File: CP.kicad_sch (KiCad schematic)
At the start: 26 parts, among them J5 Screw_Terminal_01x03, U11 OPA2991IDR, U6 OPA2991IDR

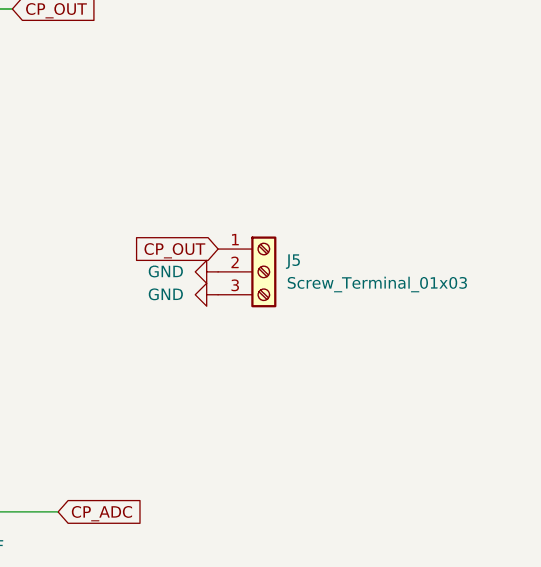
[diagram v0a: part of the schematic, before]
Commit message: 1st test board manufacturing files
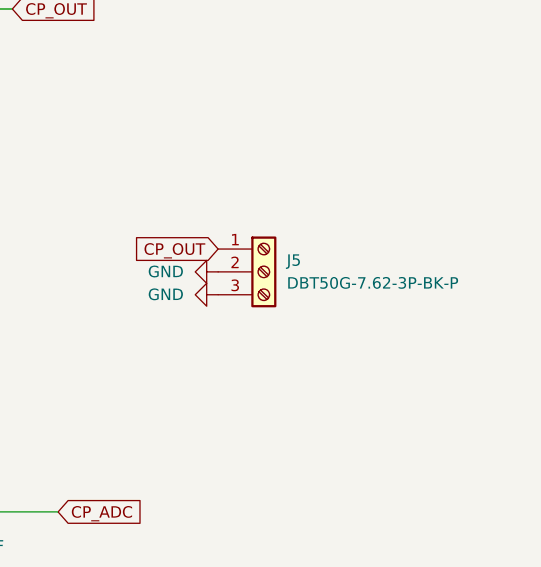
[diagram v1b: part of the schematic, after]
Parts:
- J5: value Screw_Terminal_01x03 -> DBT50G-7.62-3P-BK-P
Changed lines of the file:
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@@
 			)
 		)
-		(property "Value" "Screw_Terminal_01x03"
+		(property "Value" "DBT50G-7.62-3P-BK-P"
 			(at 254 88.8999 0)
 			(effects
